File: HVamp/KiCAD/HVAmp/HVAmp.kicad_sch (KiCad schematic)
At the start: 7 parts, among them J1 Conn_Coaxial, U1 TL071

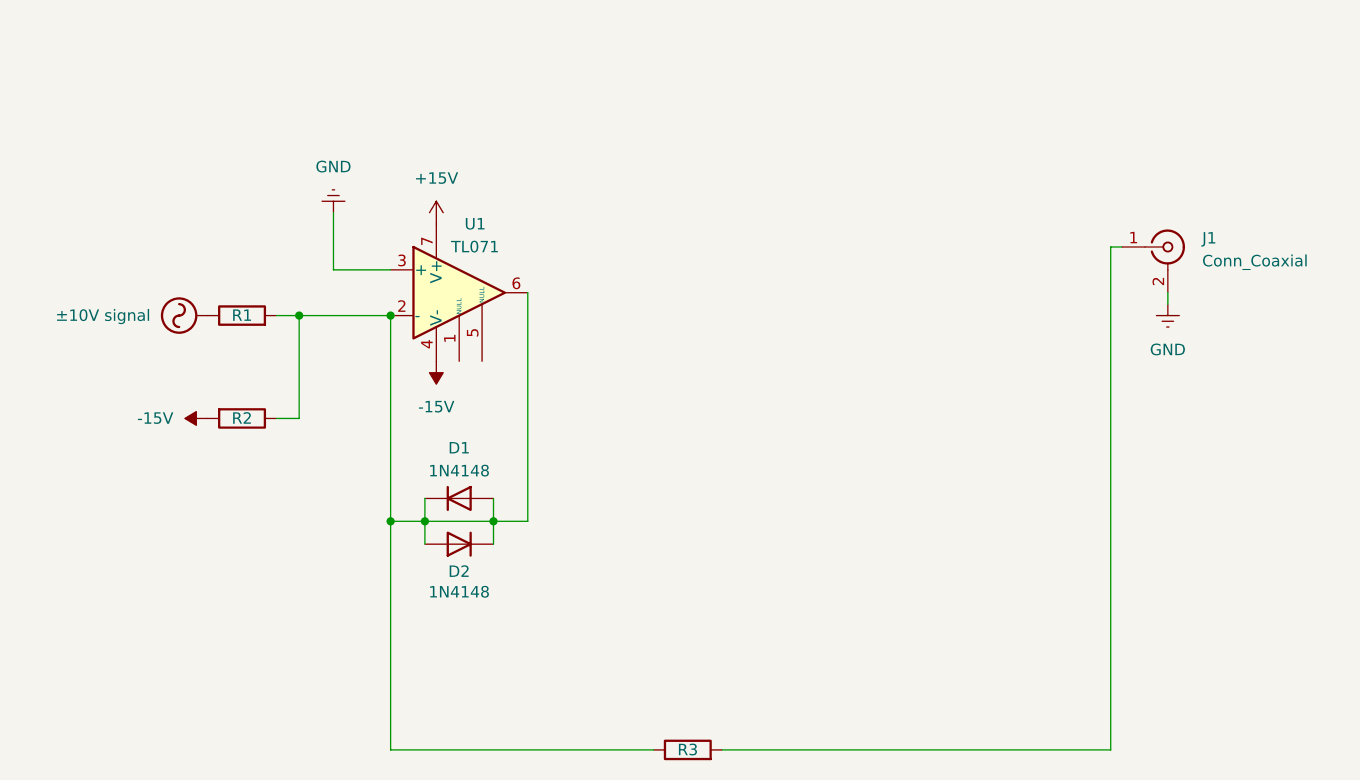
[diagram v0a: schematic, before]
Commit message: Finished KiCadschem for HVAmp
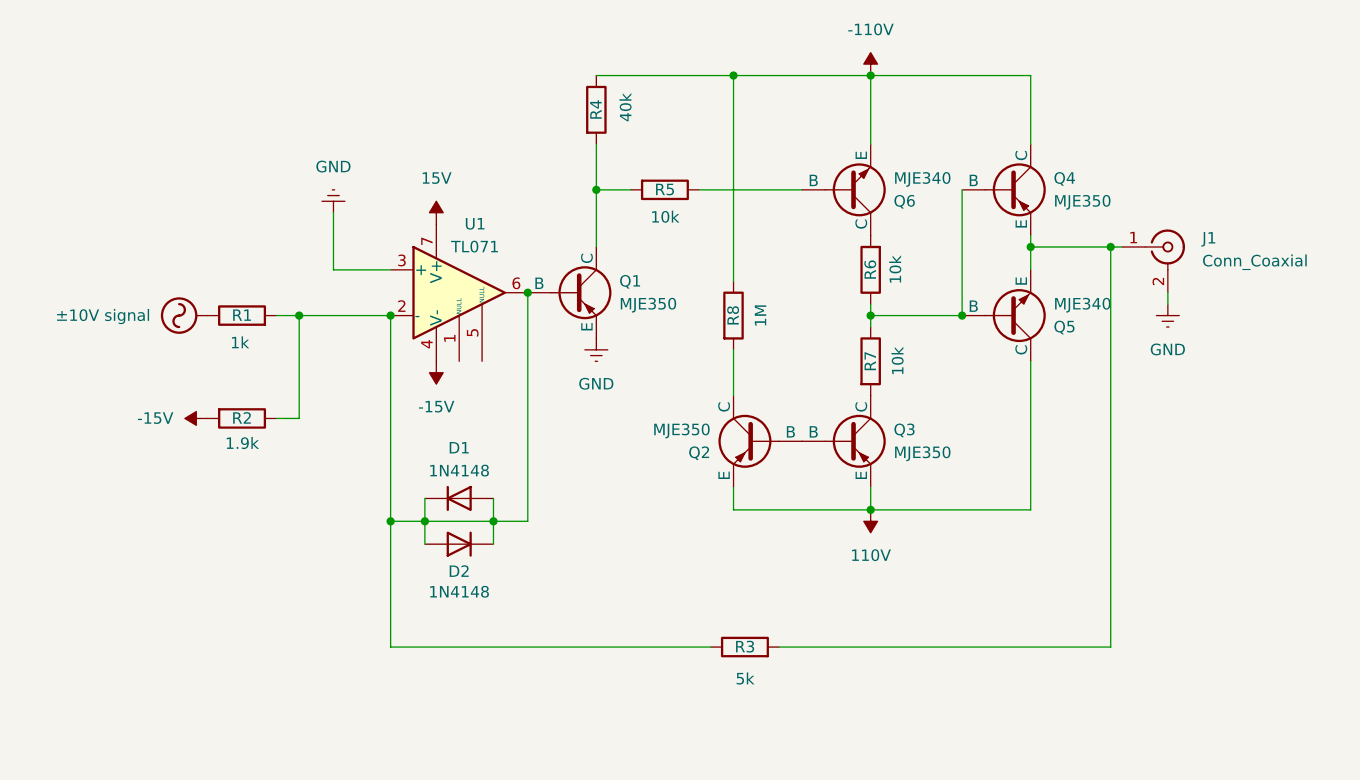
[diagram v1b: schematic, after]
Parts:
- added Q1, Q2, Q3, Q4: MJE350, symbol Simulation_SPICE:PNP
- added Q5, Q6: MJE340, symbol Simulation_SPICE:NPN
- added R4: 40k, symbol Device:R
- added R5, R6, R7: 10k, symbol Device:R
- added R8: 1M, symbol Device:R
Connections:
- net GND: now also Q1.3 (E)
- net at D1.1 (K), D1.2 (A), D2.1 (K)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: now also Q1.2 (B)
- net at J1.1 (In), R3.2: now also Q4.3 (E), Q5.3 (E)
- net +15V renamed 15V
- new net: Q2.1 (C), R8.2
- new net: Q6.1 (C), R6.2
- new net: Q6.2 (B), R5.1
- new net: Q4.2 (B), Q5.2 (B), R6.1, R7.1
- new net: Q1.1 (C), R4.2, R5.2
- new net: Q3.1 (C), R7.2
- new net: Q2.2 (B), Q3.2 (B)
- new net -110V: Q4.1 (C), Q6.3 (E), R4.1, R8.1
- new net 110V: Q2.3 (E), Q3.3 (E), Q5.1 (C)
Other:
- moved on the sheet: R3

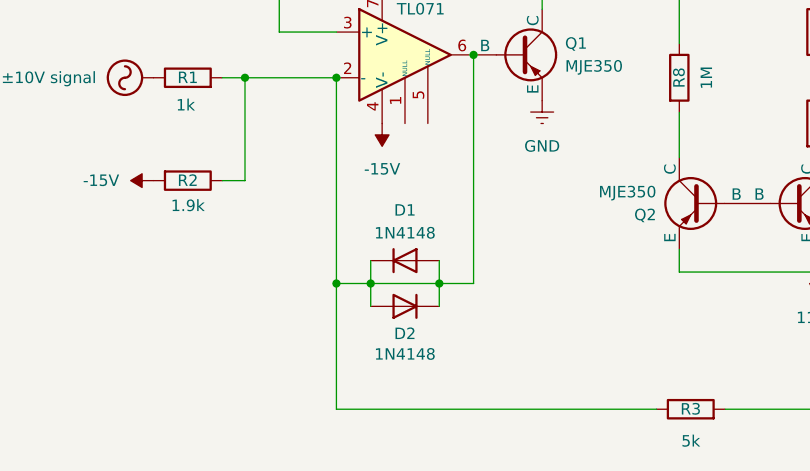
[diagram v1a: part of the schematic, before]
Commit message: Corrected HVAmp Schema
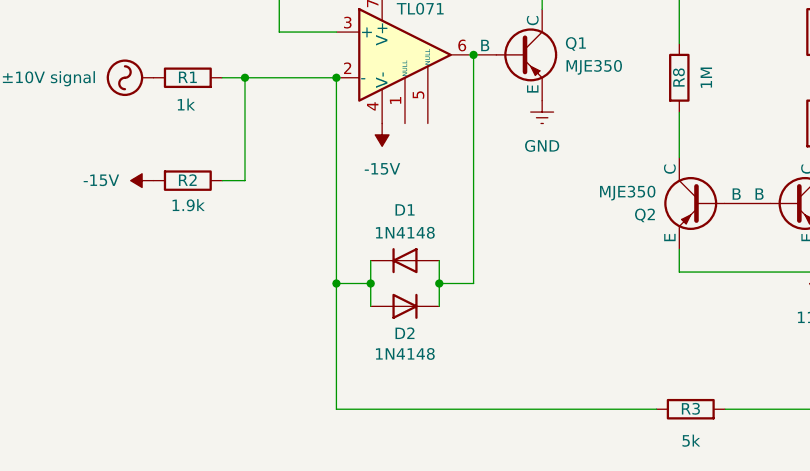
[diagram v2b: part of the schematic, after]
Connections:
- net at D1.1 (K), D2.2 (A), R1.2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: no longer D1.2 (A), D2.1 (K), Q1.2 (B), U1.6
- new net: D1.2 (A), D2.1 (K), Q1.2 (B), U1.6
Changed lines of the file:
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@@
-	(wire
-		(pts
-			(xy 90.17 81.28) (xy 82.55 81.28)
-		)
-		(stroke
-			(width 0)
-			(type default)
-		)
-	)
 	(wire
 		(pts
